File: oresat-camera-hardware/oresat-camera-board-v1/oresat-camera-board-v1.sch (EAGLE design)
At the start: 43 parts, among them J1 4-1734742-0, U1 AR0134CSSM00SPCA0, U2 TPS70618DRVR, U3 TPS71928-28DRVT, U4 TPS71928-28DRVT, X1 KC2520B27.0000C10E00

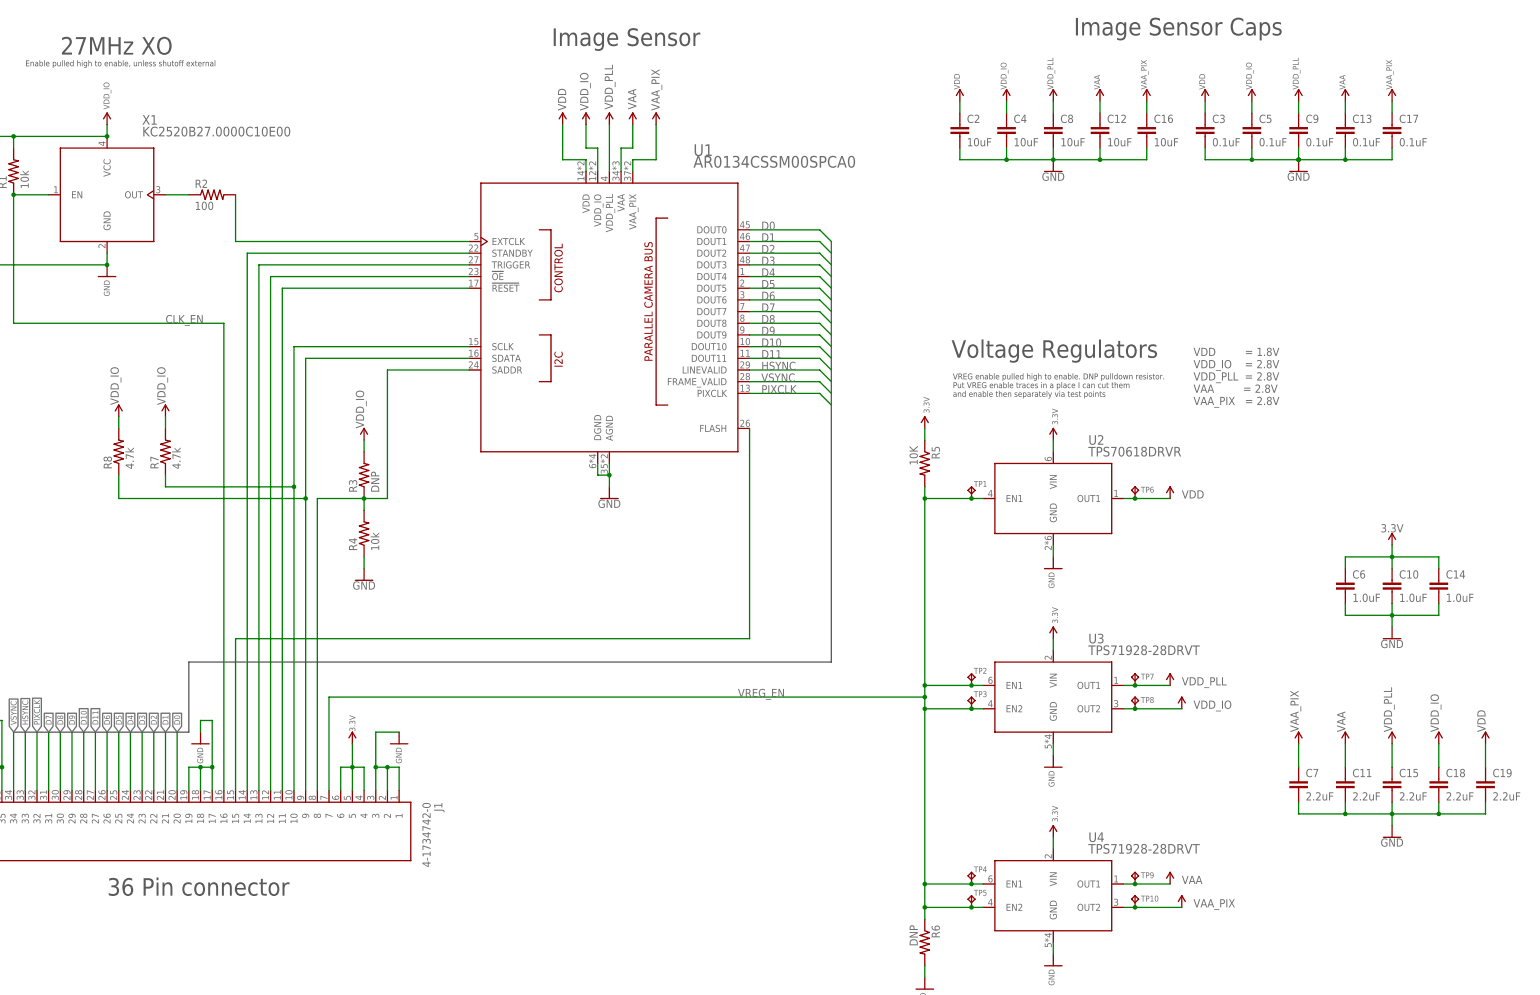
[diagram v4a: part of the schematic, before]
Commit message: fixed some ERC errors
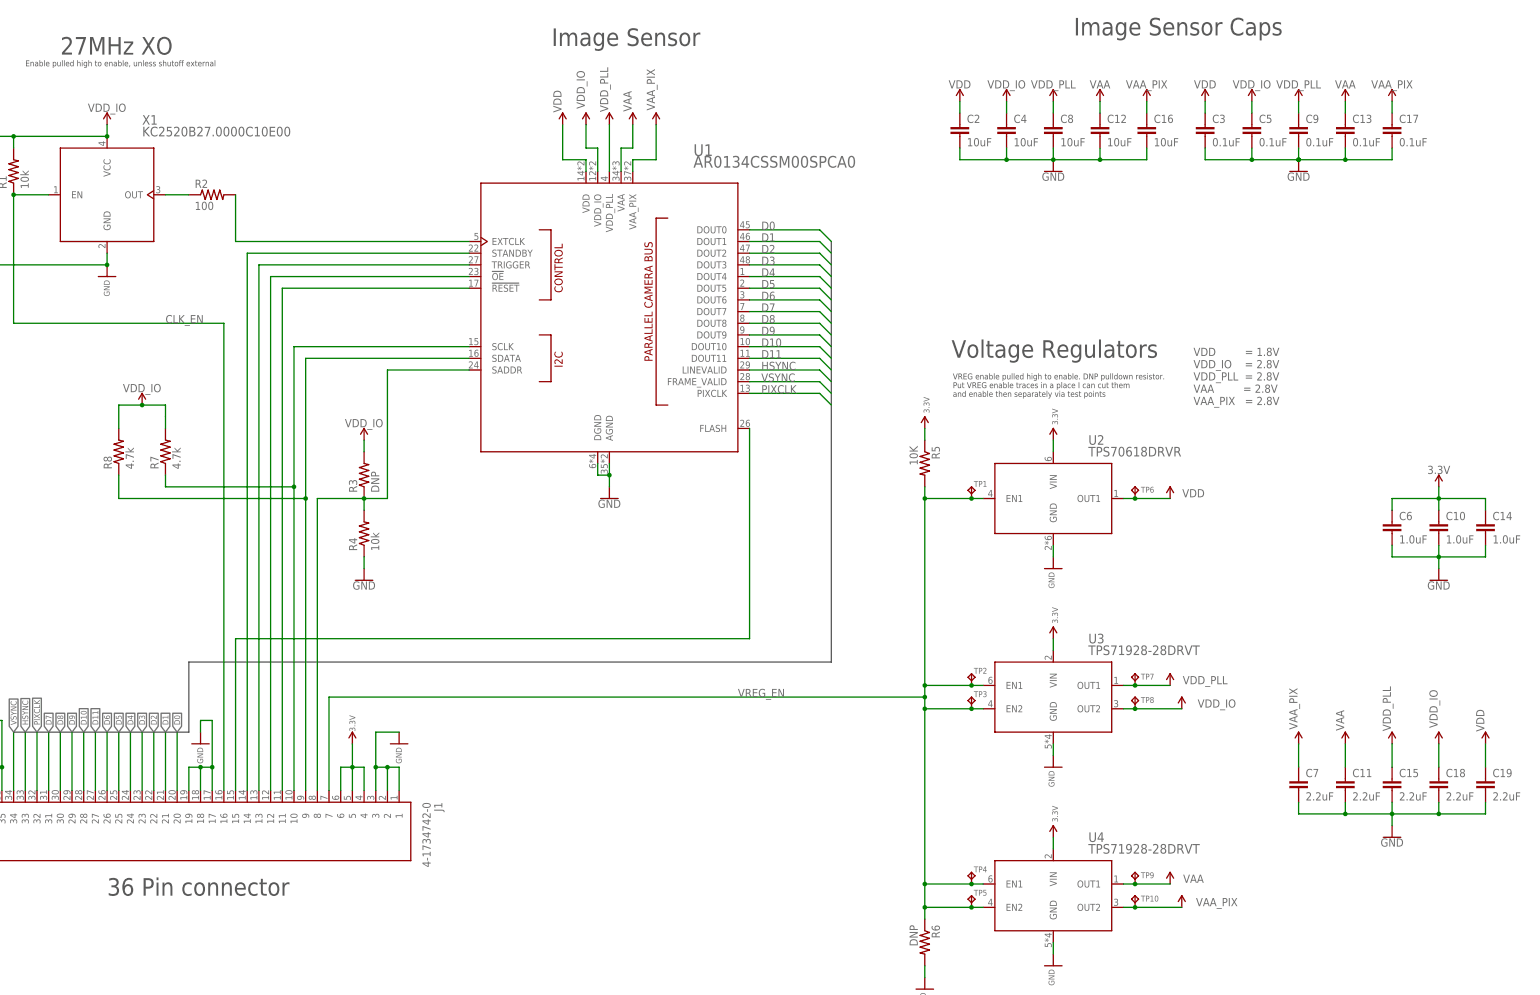
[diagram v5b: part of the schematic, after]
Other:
- moved on the sheet: C10, C14, C6
